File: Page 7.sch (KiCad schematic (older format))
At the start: 0 parts

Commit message: Updates
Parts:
- added C701, C704: 0.1uF, Capacitor_SMD:C_0603_1608Metric_Pad1.05x0.95mm_HandSolder, symbol Device:C
- added C702: 6.8nF, Capacitor_SMD:C_0603_1608Metric_Pad1.05x0.95mm_HandSolder, symbol Device:C
- added C703: 0.12uF, Capacitor_SMD:C_0805_2012Metric_Pad1.15x1.40mm_HandSolder, symbol Device:C
- added C705, C706: 10pF, Capacitor_SMD:C_0603_1608Metric_Pad1.05x0.95mm_HandSolder, symbol Device:C
- added R701, R702: R10K0, Resistor_SMD:R_0603_1608Metric_Pad1.05x0.95mm_HandSolder, symbol Device:R
- added TP701: TP_nRST, Connector_Wire:SolderWirePad_1x01_SMD_5x10mm, symbol Connector:TestPoint
- added TP702: TP_IMU_INT, Connector_Wire:SolderWirePad_1x01_SMD_5x10mm, symbol Connector:TestPoint
- added TP703: TP_SDA, Connector_Wire:SolderWirePad_1x01_SMD_5x10mm, symbol Connector:TestPoint
- added TP704: TP_SCL, Connector_Wire:SolderWirePad_1x01_SMD_5x10mm, symbol Connector:TestPoint
- added U701: BNO055, Package_LGA:LGA-28_5.2x3.8mm_P0.5mm, symbol Sensor_Motion:BNO055
- added Y701: 32.7680 kHz, Name Plate Class Project:Oscillator_MC-405_32.7680K-D__ROHS, symbol Name~Plate~Class~Library:Oscillator_MC-405_32.7680K-D__ROHS
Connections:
- net labels added: +3.3V, BNO055_INT, BNO055_SCL, BNO055_SDA, BNO055_nRST, GND, IMU_INT, SCL, SDA
- wire segments 0 -> 69
- no-connect marks 0 -> 1
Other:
- note added: "Inertial Measurement Unit"

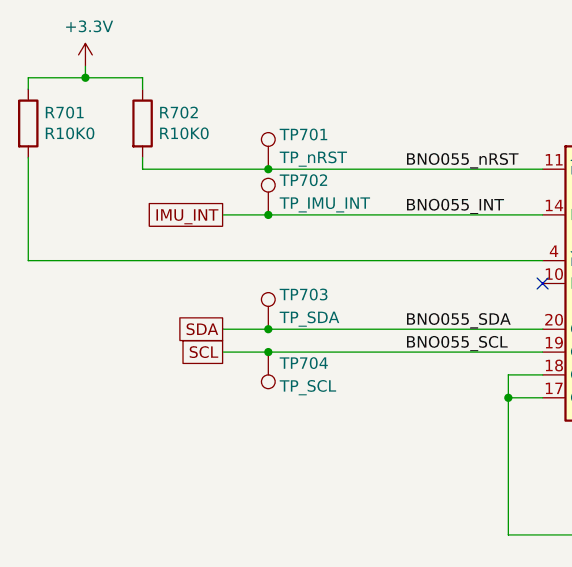
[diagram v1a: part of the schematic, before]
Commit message: Switched to Hierarchical
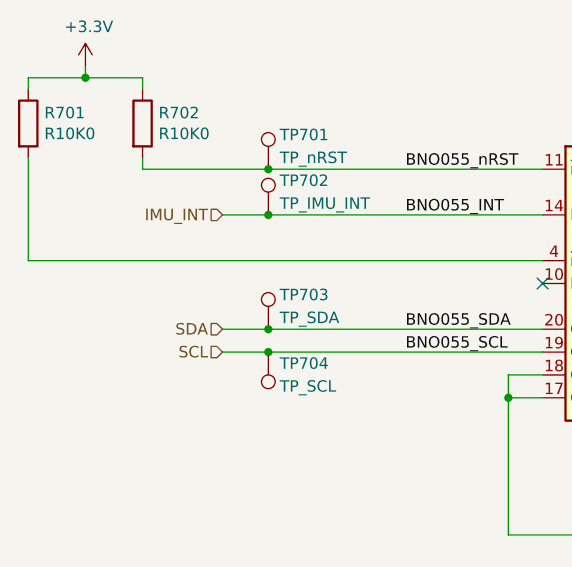
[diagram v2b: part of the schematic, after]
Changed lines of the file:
@@
 Wire Wire Line
 	5200 3450 4000 3450
-Text GLabel 3800 4250 0    50   UnSpc ~ 0
-SCL
-Text GLabel 3800 4150 0    50   UnSpc ~ 0
-SDA
-Text GLabel 3800 3650 0    50   UnSpc ~ 0
-IMU_INT
 $Comp
 L Connector:TestPoint TP?
@@
 Wire Wire Line
 	5800 3150 5800 2350
+Text HLabel 3800 3650 0    50   Input ~ 0
+IMU_INT
+Text HLabel 3800 4150 0    50   Input ~ 0
+SDA
+Text HLabel 3800 4250 0    50   Input ~ 0
+SCL
 $EndSCHEMATC
